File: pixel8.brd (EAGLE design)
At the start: 39.5 x 46 mm, 49 parts, among them CON1 DS1066-07M-SIDE, CON2 DS1066-07M-SIDE, CON3 PINHEAD_1X02-2.54, IC4 ST3485SOIC8, IC6 MC74VHC1GT125, IC7 MC74VHC1GT125

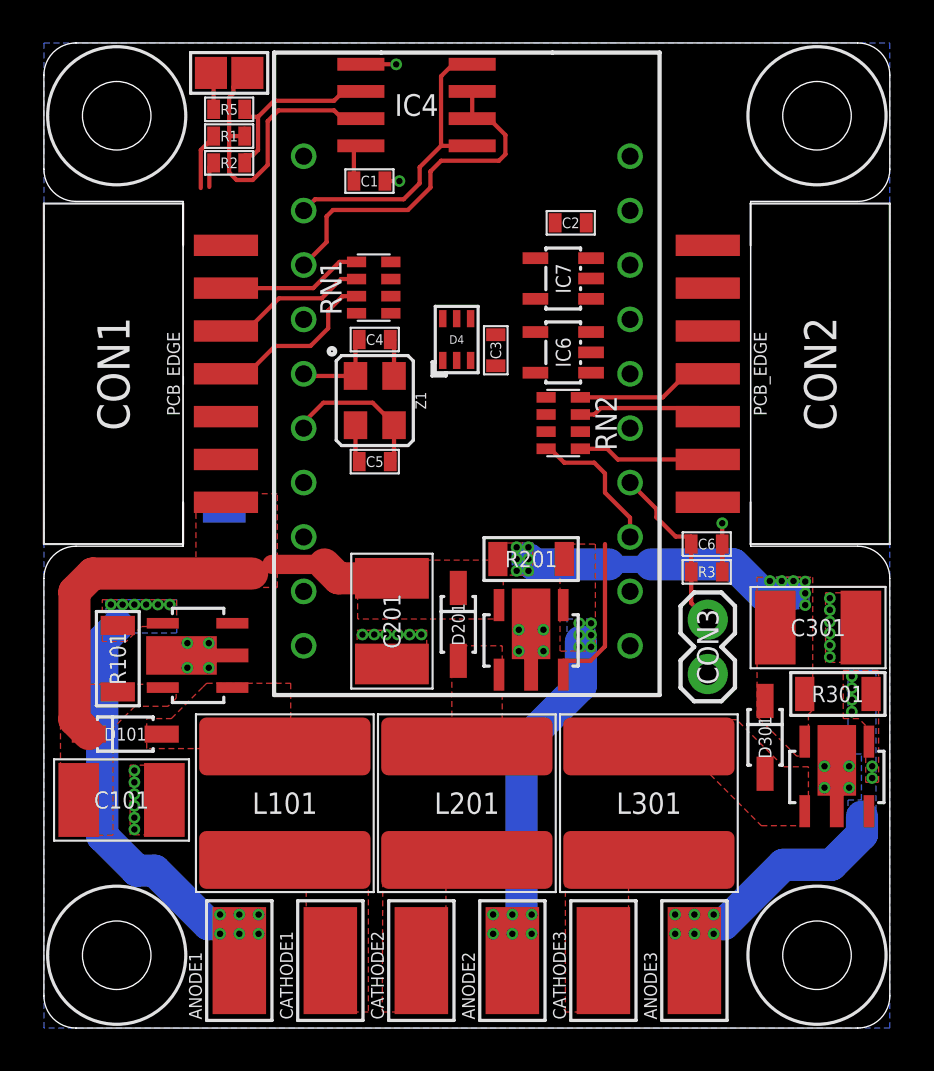
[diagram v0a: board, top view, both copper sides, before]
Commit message: added reset pad
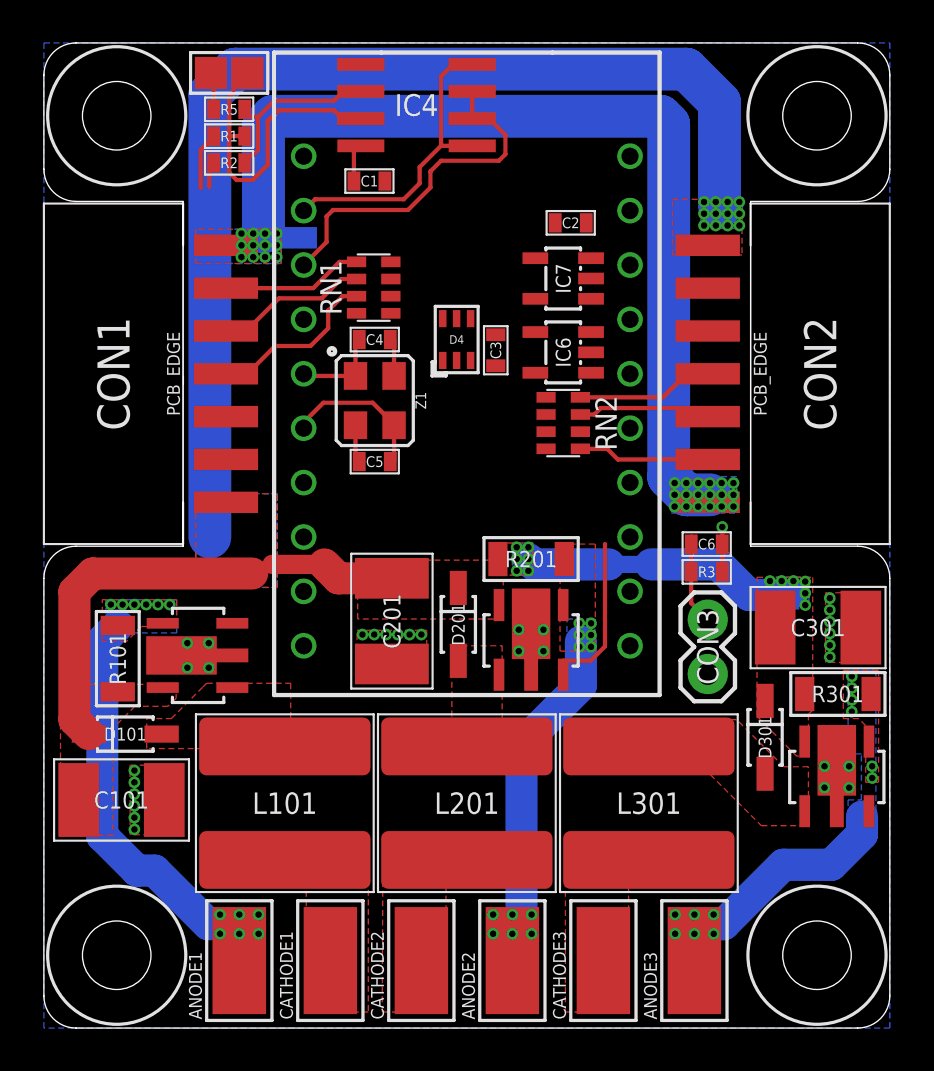
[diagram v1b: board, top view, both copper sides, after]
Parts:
- moved U$6 13.2 mm to (-8.00, 13.9), turned to 180 degrees
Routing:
- net VDD_12V: track 34.3 -> 84.8 mm, vias 12 -> 24
- net GNDD: track 0.00 -> 43.0 mm, vias 0 -> 30
- net CS_OUT: track 6.68 -> 0.20 mm
- net TEMP: track 8.33 -> 4.20 mm
- net GND: track 19.6 -> 17.1 mm, vias 33 -> 31
- added copper zone on layer 1, net GNDD
- added copper zone on layer 16, net GNDD

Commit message: -blah
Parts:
- added CON15: (no value), led_matrix_master_lib:B2B-PH-K-S_SIDE_MOUNT
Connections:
- new net VDD_24V: CON15.2
- net GND: now also CON15.1
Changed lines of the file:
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@@
 <grid distance="0.025" unitdist="mm" unit="mm" style="lines" multiple="2" display="yes" altdistance="0.5" altunitdist="mm" altunit="mm"/>
 <layers>
-<layer number="1" name="Top" color="4" fill="1" visible="no" active="yes"/>
+<layer number="1" name="Top" color="4" fill="1" visible="yes" active="yes"/>
 <layer number="2" name="Route2" color="1" fill="3" visible="no" active="no"/>
 <layer number="3" name="Route3" color="4" fill="3" visible="no" active="no"/>
@@
 <layer number="19" name="Unrouted" color="6" fill="1" visible="yes" active="yes"/>
 <layer number="20" name="Dimension" color="15" fill="1" visible="yes" active="yes"/>
-<layer number="21" name="tPlace" color="7" fill="1" visible="no" active="yes"/>
+<layer number="21" name="tPlace" color="7" fill="1" visible="yes" active="yes"/>
 <layer number="22" name="bPlace" color="7" fill="1" visible="yes" active="yes"/>
-<layer number="23" name="tOrigins" color="15" fill="1" visible="no" active="yes"/>
+<layer number="23" name="tOrigins" color="15" fill="1" visible="yes" active="yes"/>
 <layer number="24" name="bOrigins" color="15" fill="1" visible="yes" active="yes"/>
-<layer number="25" name="tNames" color="7" fill="1" visible="no" active="yes"/>
+<layer number="25" name="tNames" color="7" fill="1" visible="yes" active="yes"/>
 <layer number="26" name="bNames" color="7" fill="1" visible="yes" active="yes"/>
 <layer number="27" name="tValues" color="7" fill="1" visible="no" active="yes"/>
@@
 <layer number="49" name="Reference" color="7" fill="1" visible="yes" active="yes"/>
 <layer number="50" name="dxf" color="7" fill="1" visible="no" active="no"/>
-<layer number="51" name="tDocu" color="7" fill="1" visible="no" active="yes"/>
+<layer number="51" name="tDocu" color="7" fill="1" visible="yes" active="yes"/>
 <layer number="52" name="bDocu" color="7" fill="1" visible="yes" active="yes"/>
 <layer number="53" name="tGND_GNDA" color="7" fill="9" visible="no" active="no"/>
@@
 <layer number="220" name="220bmp" color="21" fill="1" visible="no" active="no"/>
 <layer number="221" name="221bmp" color="22" fill="1" visible="no" active="no"/>
+<layer number="222" name="222bmp" color="23" fill="1" visible="no" active="no"/>
 <layer number="223" name="223bmp" color="24" fill="1" visible="no" active="no"/>
 <layer number="224" name="224bmp" color="25" fill="1" visible="no" active="no"/>
@@
 <element name="U$4" library="pixel_masterlib" package="MOUNTING_HOLE_M3" value="" x="16.35" y="19.6"/>
 <element name="U$5" library="pixel_masterlib" package="MOUNTING_HOLE_M3" value="" x="-16.35" y="19.6"/>
+<element name="CON15" library="led_matrix_master_lib" package="B2B-PH-K-S_SIDE_MOUNT" value="" x="3.775" y="17.025"/>
 </elements>
 <signals>
@@
 <wire x1="-13.325" y1="-5.6" x2="-13.05" y2="-5.325" width="0.2" layer="1"/>
 <wire x1="-13.05" y1="-5.325" x2="-13.05" y2="-5.025" width="0.2" layer="1"/>
+<contactref element="CON15" pad="1"/>
 <wire x1="-3.825" y1="16.55" x2="-4.95" y2="22.005" width="0" layer="19" extent="1-1"/>
 <wire x1="-7.5" y1="13.9" x2="-3.825" y2="16.55" width="0" layer="19" extent="1-16"/>
@@
 <wire x1="5.8" y1="12.95" x2="5.8" y2="9.5" width="0" layer="19" extent="1-1"/>
 <wire x1="4.125" y1="14.6" x2="5.8" y2="12.95" width="0" layer="19" extent="1-1"/>
+<wire x1="2.775" y1="14.875" x2="4.125" y2="14.6" width="0" layer="19" extent="1-1"/>
 </signal>
 <signal name="TEMP">
@@
 <wire x1="-1.205" y1="21.445" x2="-1.205" y2="18.195" width="0.2" layer="1"/>
 </signal>
+<signal name="VDD_24V">
+<contactref element="CON15" pad="2"/>
+</signal>
 </signals>
